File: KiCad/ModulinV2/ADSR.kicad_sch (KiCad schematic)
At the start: 57 parts, among them IC30 TL074HIDR, IC34 AS3310D, IC38 AS3310D

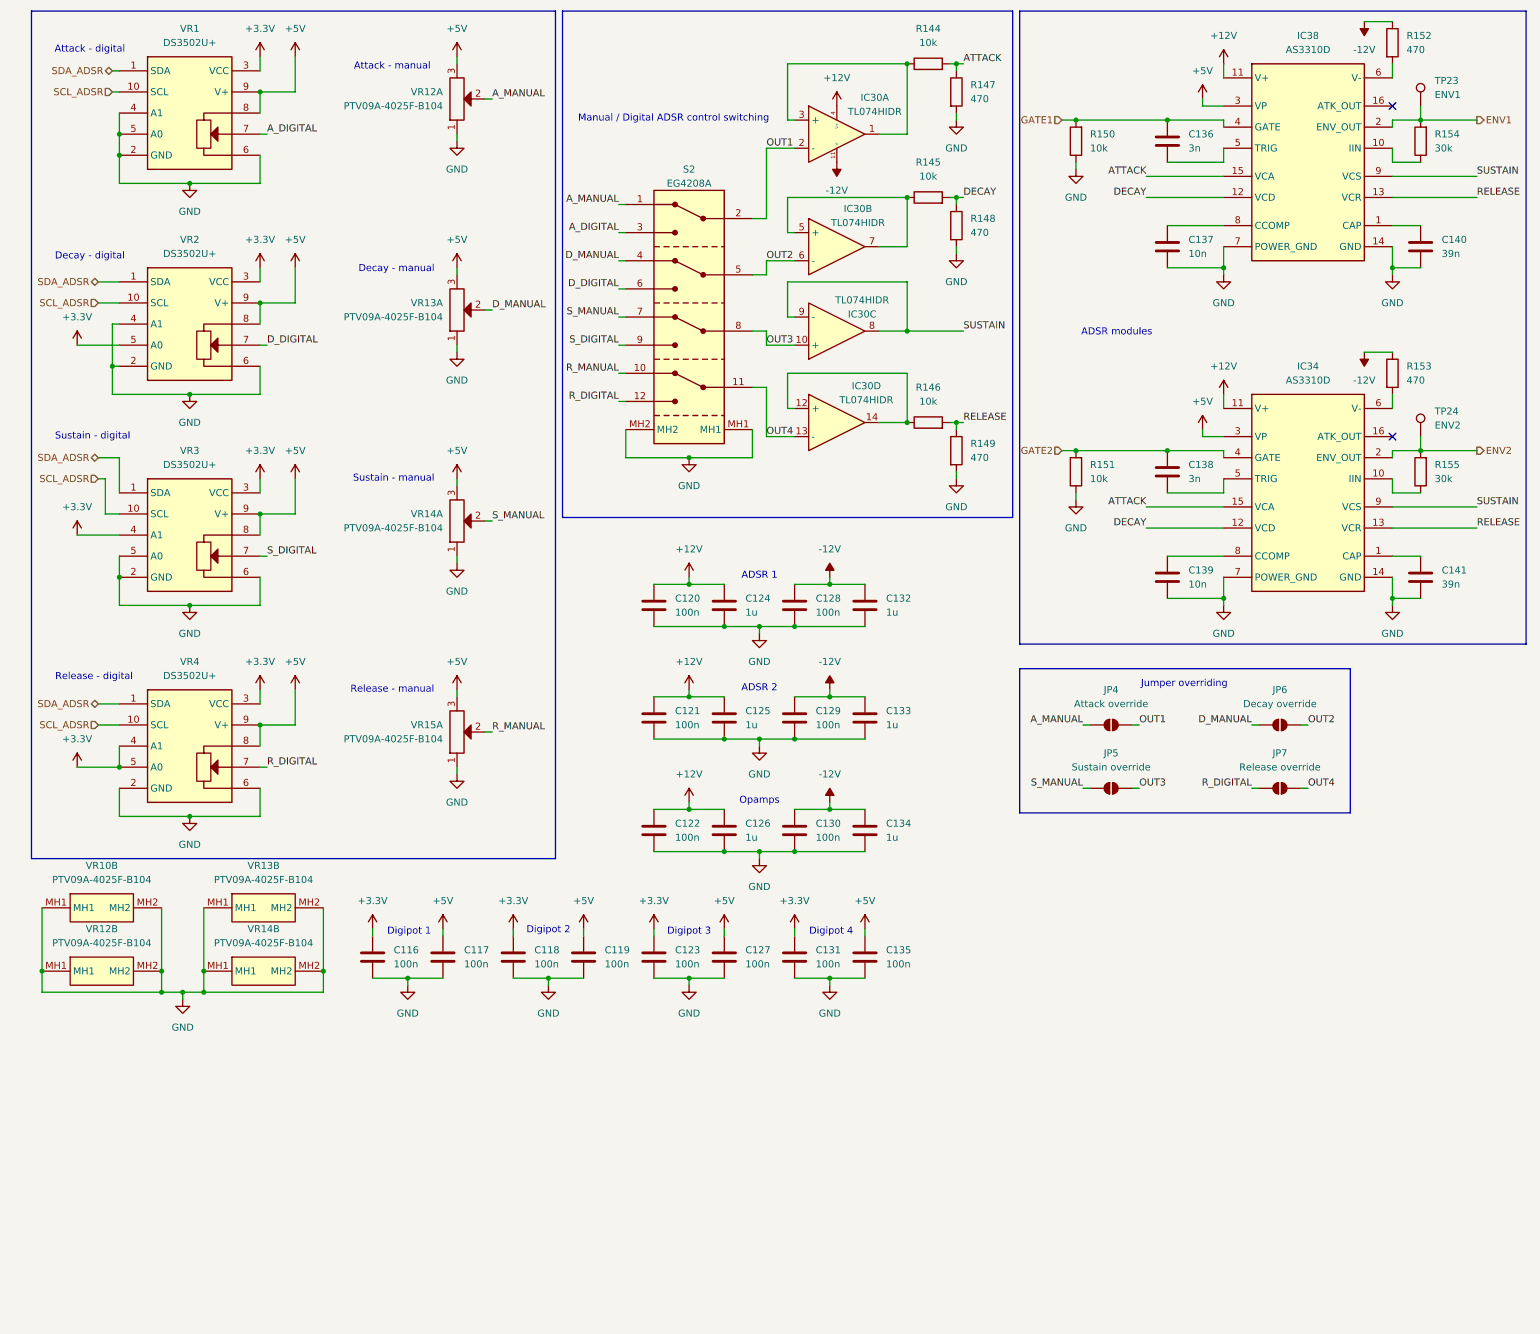
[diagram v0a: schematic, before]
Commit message: Changed switch for the boot and nrst. Fixed the GATE interface trigger
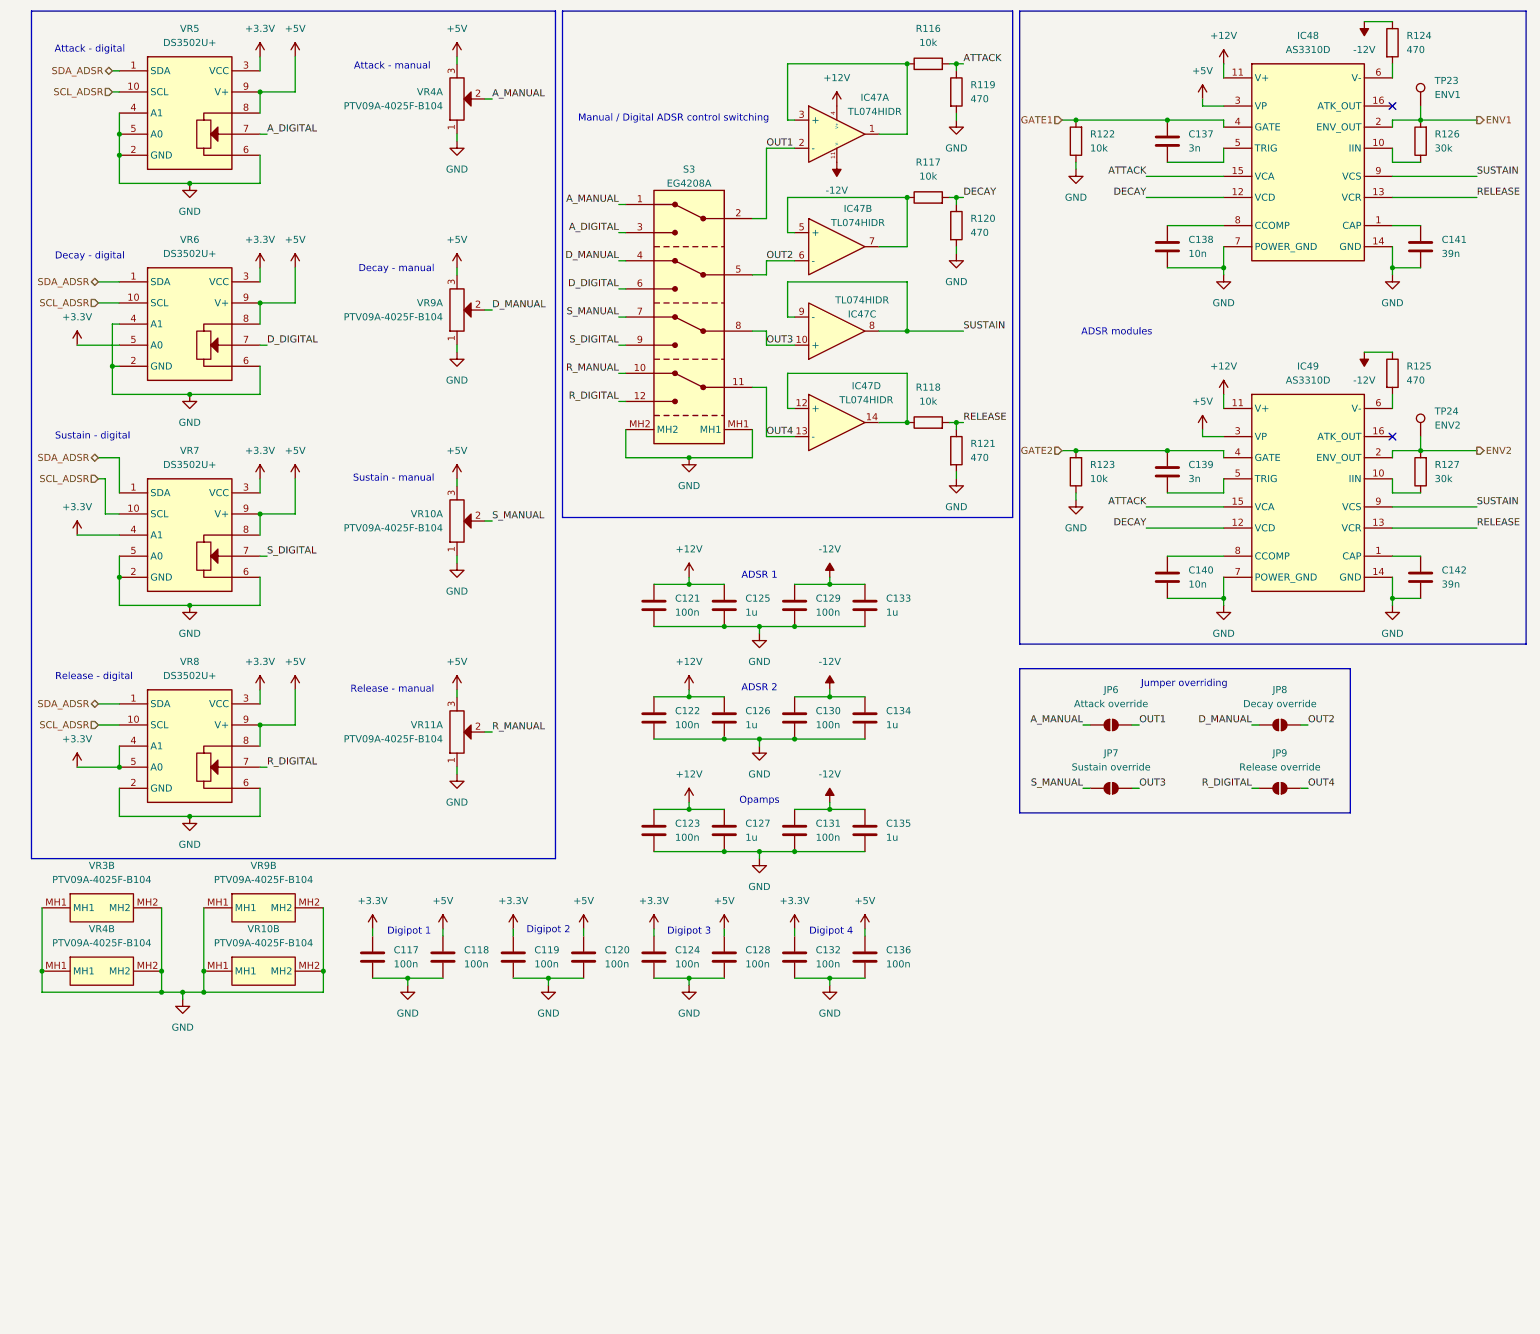
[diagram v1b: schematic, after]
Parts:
- renumbered C116 to C117, C117 to C118, C118 to C119, C119 to C120, C120 to C121, C121 to C122, C122 to C123, C123 to C124, C124 to C125, C125 to C126, C126 to C127, C127 to C128, C128 to C129, C129 to C130, C130 to C131, C131 to C132, C132 to C133, C133 to C134, C134 to C135, C135 to C136, C136 to C137, C137 to C138, C138 to C139, C139 to C140, C140 to C141, C141 to C142, IC30 to IC47, IC38 to IC48, IC34 to IC49, JP4 to JP6, JP5 to JP7, JP6 to JP8, JP7 to JP9, R144 to R116, R145 to R117, R146 to R118, R147 to R119, R148 to R120, R149 to R121, R150 to R122, R151 to R123, R152 to R124, R153 to R125, R154 to R126, R155 to R127, S2 to S3, VR14 to VR10, VR15 to VR11, VR10 to VR3, VR12 to VR4, VR1 to VR5, VR2 to VR6, VR3 to VR7, VR4 to VR8, VR13 to VR9

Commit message: Started adding footprints for capacitors
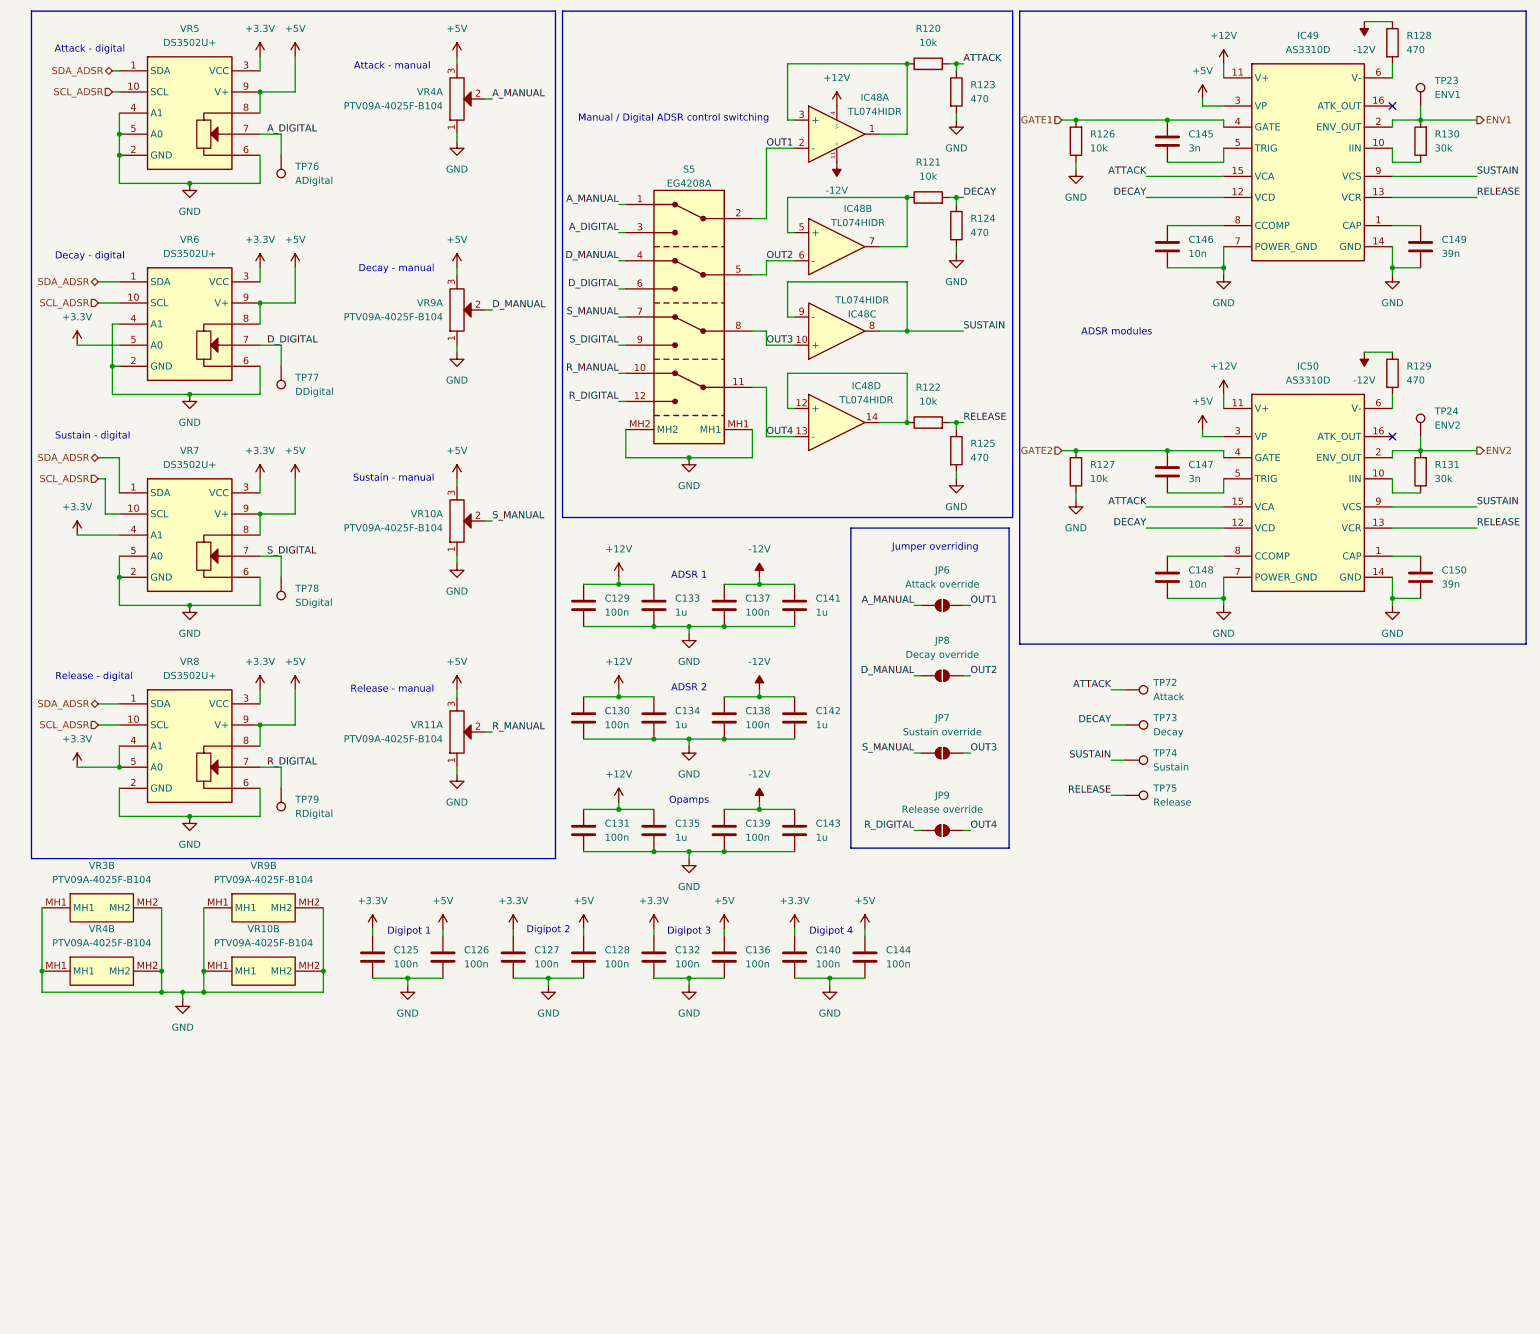
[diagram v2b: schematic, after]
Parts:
- added TP72: Attack, SamacSys_Parts:TestPointLoop, symbol Connector:TestPoint
- added TP73: Decay, SamacSys_Parts:TestPointLoop, symbol Connector:TestPoint
- added TP74: Sustain, SamacSys_Parts:TestPointLoop, symbol Connector:TestPoint
- added TP75: Release, SamacSys_Parts:TestPointLoop, symbol Connector:TestPoint
- added TP76: ADigital, SamacSys_Parts:TestPointLoop, symbol Connector:TestPoint
- added TP77: DDigital, SamacSys_Parts:TestPointLoop, symbol Connector:TestPoint
- added TP78: SDigital, SamacSys_Parts:TestPointLoop, symbol Connector:TestPoint
- added TP79: RDigital, SamacSys_Parts:TestPointLoop, symbol Connector:TestPoint
- C125: renamed from C117; footprint (none) -> SamacSys_Parts:CAPC1608X90N
- C126: renamed from C118; footprint (none) -> SamacSys_Parts:CAPC1608X90N
- C127: renamed from C119; footprint (none) -> SamacSys_Parts:CAPC1608X90N
- C128: renamed from C120; footprint (none) -> SamacSys_Parts:CAPC1608X90N
- C129: renamed from C121; footprint (none) -> SamacSys_Parts:CAPC1608X90N
- C130: renamed from C122; footprint (none) -> SamacSys_Parts:CAPC1608X90N
- C131: renamed from C123; footprint (none) -> SamacSys_Parts:CAPC1608X90N
- C132: renamed from C124; footprint (none) -> SamacSys_Parts:CAPC1608X90N
- C133: renamed from C125; footprint (none) -> SamacSys_Parts:CAPC1608X95N
- C134: renamed from C126; footprint (none) -> SamacSys_Parts:CAPC1608X95N
- C135: renamed from C127; footprint (none) -> SamacSys_Parts:CAPC1608X95N
- C136: renamed from C128; footprint (none) -> SamacSys_Parts:CAPC1608X90N
- C137: renamed from C129; footprint (none) -> SamacSys_Parts:CAPC1608X90N
- C138: renamed from C130; footprint (none) -> SamacSys_Parts:CAPC1608X90N
- C139: renamed from C131; footprint (none) -> SamacSys_Parts:CAPC1608X90N
- C140: renamed from C132; footprint (none) -> SamacSys_Parts:CAPC1608X90N
- C141: renamed from C133; footprint (none) -> SamacSys_Parts:CAPC1608X95N
- C142: renamed from C134; footprint (none) -> SamacSys_Parts:CAPC1608X95N
- C143: renamed from C135; footprint (none) -> SamacSys_Parts:CAPC1608X95N
- C144: renamed from C136; footprint (none) -> SamacSys_Parts:CAPC1608X90N
- C146: renamed from C138; footprint (none) -> SamacSys_Parts:CAPC1608X90N
- C148: renamed from C140; footprint (none) -> SamacSys_Parts:CAPC1608X90N
- TP23, TP24: footprint (none) -> SamacSys_Parts:TestPointLoop
- renumbered C137 to C145, C139 to C147, C141 to C149, C142 to C150, IC47 to IC48, IC48 to IC49, IC49 to IC50, R116 to R120, R117 to R121, R118 to R122, R119 to R123, R120 to R124, R121 to R125, R122 to R126, R123 to R127, R124 to R128, R125 to R129, R126 to R130, R127 to R131, S3 to S5
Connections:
- net ATTACK: now also TP72.1
- net A_DIGITAL: now also TP76.1
- net DECAY: now also TP73.1
- net D_DIGITAL: now also TP77.1
- net RELEASE: now also TP75.1
- net R_DIGITAL: now also TP79.1
- net SUSTAIN: now also TP74.1
- net S_DIGITAL: now also TP78.1
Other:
- moved on the sheet: C129, C130, C131, C133, C134, C135, C137, C138, C139, C141, C142, C143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
